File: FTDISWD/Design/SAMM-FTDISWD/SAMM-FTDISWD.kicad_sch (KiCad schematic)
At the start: 2 parts

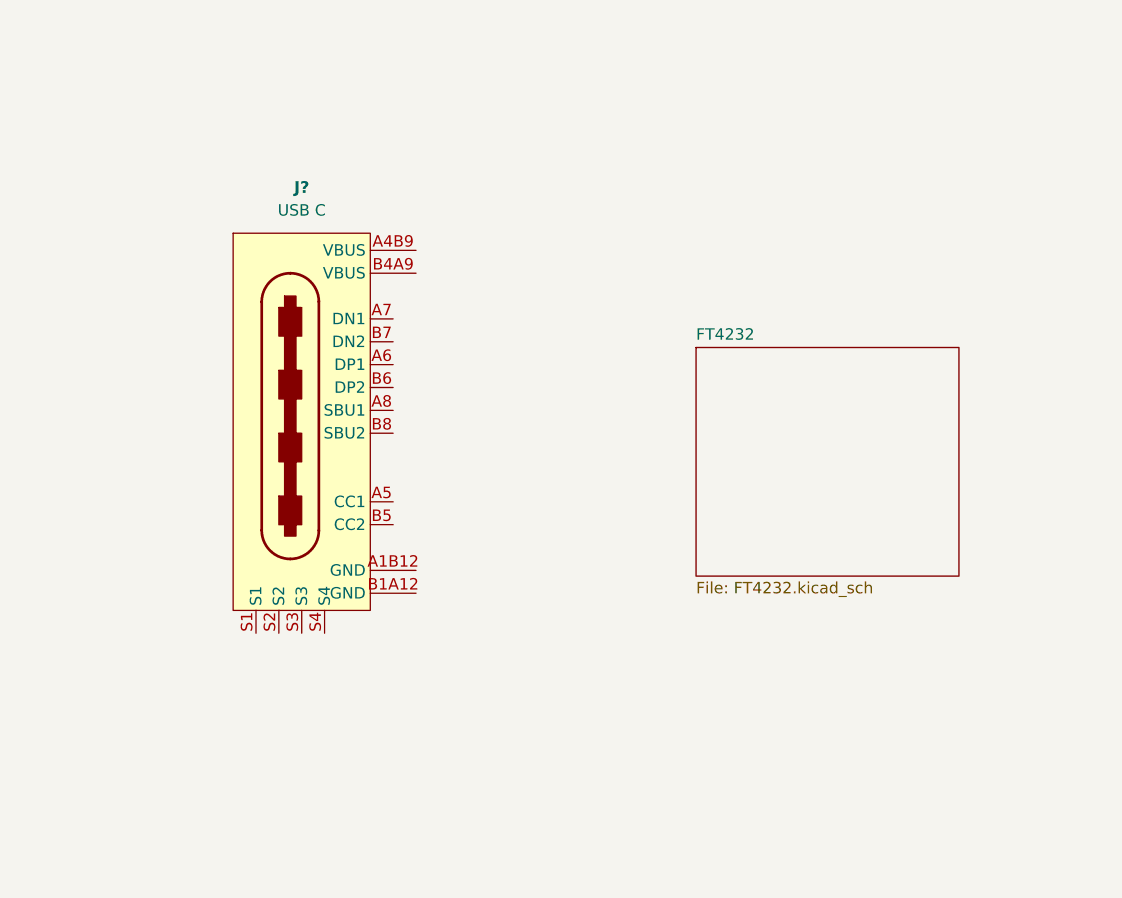
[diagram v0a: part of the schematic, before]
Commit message: SAMM-FTDISWD schematic update 1
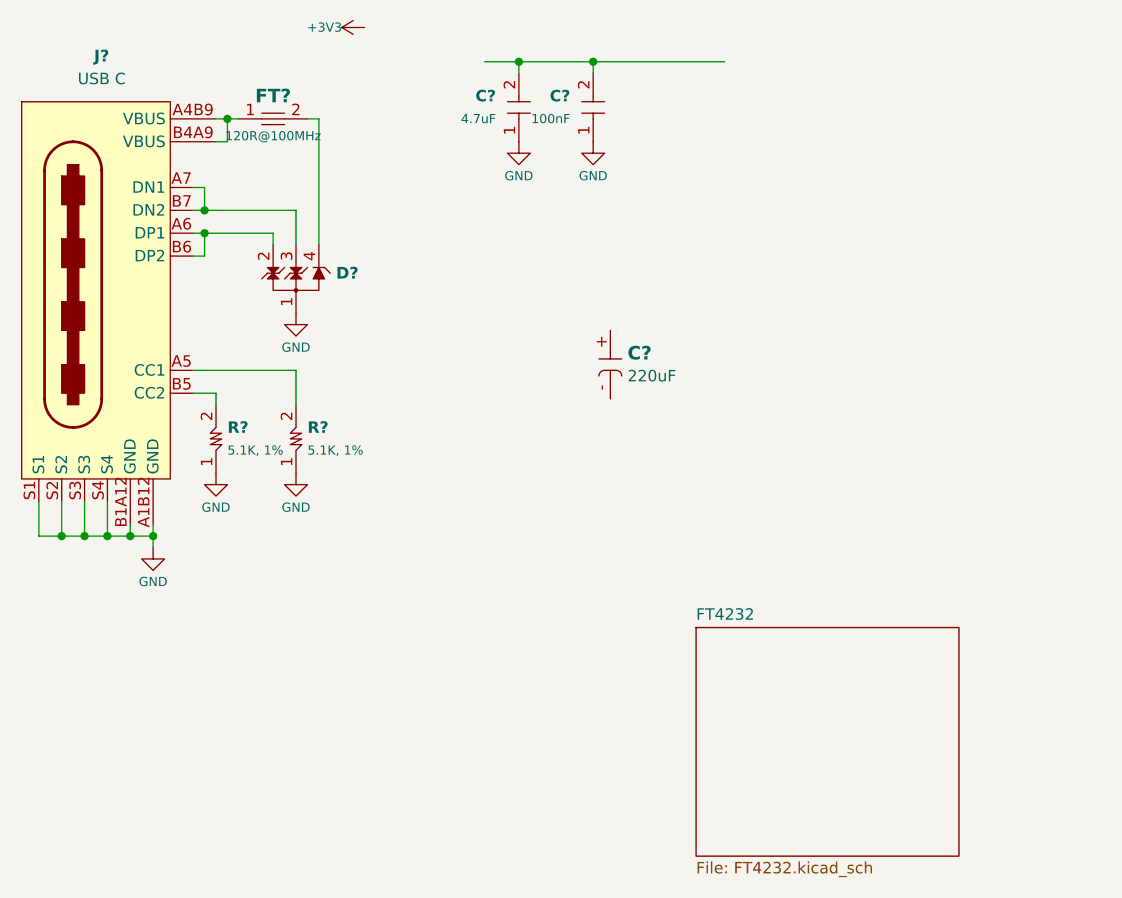
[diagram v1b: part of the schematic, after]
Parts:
- added C?: 220uF, symbol SAMPI:ELECCAP
- added C?: 100nF, Liem:CAP0402, symbol SAMPI:CERCAP
- added C?: 4.7uF, Liem:CAP0402, symbol SAMPI:CERCAP
- added D?: TVS 3-CH, SAMPI:SOT143B_NEXT, symbol SAMPI:TVS_3CH
- added FT?: 120R@100MHz, Liem:FB0402, symbol Liem:FerriteBead
- added R? (x2): 5.1K, 1%, Liem:RES0402, symbol SAMPI:RES
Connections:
- net GND: now reaches J?.A1B12 (GND)
- net GND: now also J?.B1A12 (GND), J?.S1, J?.S2, J?.S3, J?.S4, C?.1, C?.1, D?.1 (GND), R?.1, R?.1
- net at J?.A4B9 (VBUS): now also J?.B4A9 (VBUS), FT?.1
- net at J?.A5 (CC1): now also R?.2
- net at J?.A6 (DP1): now also J?.B6 (DP2), D?.2 (CH1)
- net at J?.A7 (DN1): now also J?.B7 (DN2), D?.3 (CH2)
- net at J?.B5 (CC2): now also R?.2
- new net: D?.4 (CH3), FT?.2
- new net: C?.2, C?.2

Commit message: SAMM-FTDISWD schematic update 2
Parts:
- removed U?: SN74LVC126, symbol SAMPI:SN74LVC126ABQAR
- added C? (x9): 100nF, Liem:CAP0402, symbol SAMPI:CERCAP
- added C?: 22pF, Liem:CAP0402, symbol SAMPI:CERCAP
- added H?: SWD, SAMPI:HDM-2x5x1.27-TH, symbol Liem:INP3000
- added Q? (x2): 2N-CH, Liem:TSOT26, symbol SAMPI:DMN2041
- added R? (x6): 33R, Liem:RES0402, symbol SAMPI:RES
- added R?: Rt, Liem:RES0402, symbol SAMPI:RES
- added R?: 0R, Liem:RES0402, symbol SAMPI:RES
- added R?: 1K, Liem:RES0402, symbol SAMPI:RES
- added R? (x2): 10K, Liem:RES0402, symbol SAMPI:RES
- added R?: 1M, Liem:RES0402, symbol SAMPI:RES
- added SW?: PWR SEL, SAMPI:CUS-12B, symbol Liem:SW-SLIDE
- added U? (x5): NC7SZ126, Liem:SOT353, symbol Liem:LEVEL_SHIFTER_1-CH
- added U?: LDO 3.3V/1.5A, SAMPI:DFN8_3x3_MCHP, symbol SAMPI:MCP1727
- added U?: MCP6001, symbol SAMPI:OPAMP-1CH
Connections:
- net +3V3: now also C?.2, C?.2, C?.2, C?.2, R?.1, R?.2, SW?.1 (NC), U?.5 (VCC), U?.5 (VCC), U?.8 (VOUT)
- net GND: now also C?.-, C?.1, C?.1, C?.1, C?.1, C?.1, C?.1, C?.1, C?.1, C?.1, C?.1, H?.3 (GND), H?.5 (GND), H?.9 (GND), Q?.1 (S1), Q?.3 (S2), R?.1, R?.1, SW?.4 (CH), SW?.5 (CH), U?.2 (VSS), U?.3 (GND), U?.3 (GND), U?.3 (GND), U?.3 (GND), U?.3 (GND), U?.4 (GND), U?.9 (EP)
- net +5V: now reaches D?.4 (CH3), FT?.2
- net +5V: now also C?.+, C?.2, C?.2, U?.1 (VIN), U?.2 (VIN), U?.3 (~{SHDN}), U?.5 (VDD)
- net USB_P: now reaches D?.2 (CH1), J?.A6 (DP1), J?.B6 (DP2)
- net USB_N: now reaches D?.3 (CH2), J?.A7 (DN1), J?.B7 (DN2)
- new net: Q?.5 (D21), R?.2, R?.2
- new net: R?.1, R?.2, U?.7 (SEN/ADJ)
- new net: Q?.2 (D12), Q?.4 (G2), R?.2
- new net: C?.2, R?.1, U?.1 (VIN+)
- new net: R?.2, U?.2 (INA)
- new net: R?.2, U?.4 (OUTY) (x2)
- new net: R?.2, U?.3 (VIN-), U?.4 (VOUT)
- new net: R?.2, U?.2 (INA), U?.4 (OUTY)
- new net: C?.2, U?.6 (CDELAY)
- new net FT4232/~{TARGET_RESET}: Q?.6 (G1)
- new net IO_DIR: U?.1 (OE)
- new net PWRGD: U?.5 (PWRGD)
- new net RXD: H?.7 (DB_TX), U?.4 (OUTY)
- new net SWD_EN: U?.1 (OE), U?.1 (OE)
- new net TCK: U?.2 (INA)
- new net TDI: U?.2 (INA)
- new net TDO: U?.4 (OUTY)
- new net TG_RXD: R?.1
- new net TG_SWCLK: H?.4 (SWCLK), R?.1
- new net TG_SWDIO: H?.2 (SWDIO), R?.1
- new net TG_TXD: R?.1
- new net TXD: H?.8 (DB_RX), U?.2 (INA)
- new net UART_EN: U?.1 (OE), U?.1 (OE)
- new net VIO: C?.2, C?.2, C?.2, C?.2, R?.1, R?.1, U?.5 (VCC), U?.5 (VCC), U?.5 (VCC)
- new net VTG: H?.1 (VDD), R?.2, R?.2, SW?.2 (COM), SW?.3 (NO)
- new net ~{TG_RST}: H?.10 (~{RST}), R?.1
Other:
- sheet FT4232 ports: added RXD1, SWDIO_DIR, SWD_EN, TCK, TDI, TDO, TXD1, USB_N, USB_P, ~{RESET}, ~{TARGET_RESET}; removed none
- moved on the sheet: C?
